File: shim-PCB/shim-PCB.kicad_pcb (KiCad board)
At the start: 2 copper layers, 67.5 x 95.4 mm, 22 parts, among them J1 ROMI-Encoder, J10 LineSensor, J11 LineSensor, J12 SPI, J13 Ultrasonic., J14 THING, J15 THING, J2 ROMI-Encoder, J3 Conn_01x19_Female, J4 ServoAnalog, J5 Conn_01x19_Female, J6 Conn_01x19_Female, J7 ROMI, J8 ROMI, J9 Conn_01x19_Female

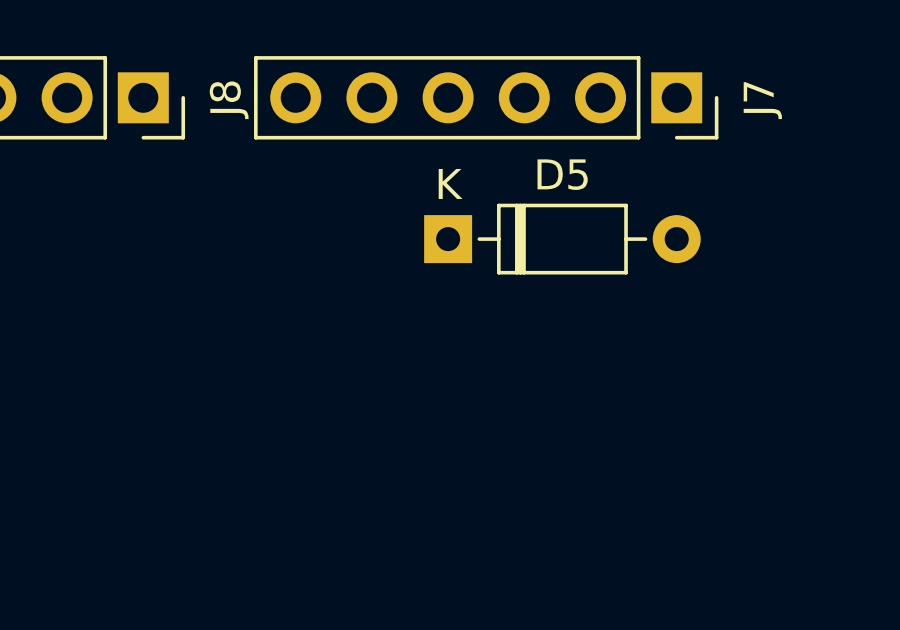
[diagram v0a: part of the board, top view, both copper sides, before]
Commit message: Clamped ~SLP pin and added 02x01 header.
Issue #13
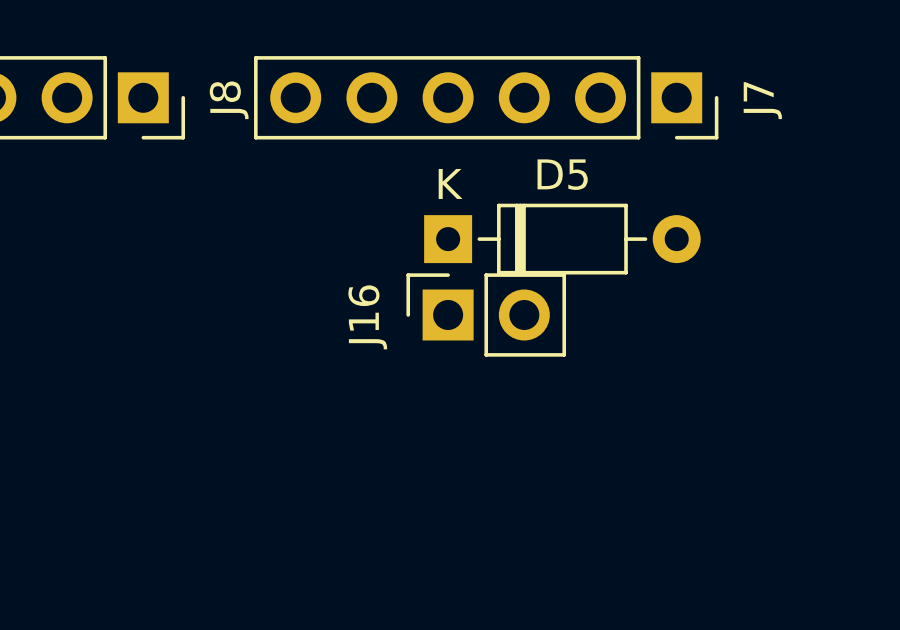
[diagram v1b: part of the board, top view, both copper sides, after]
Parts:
- added J16: Conn_01x02_Female, Connector_PinSocket_2.54mm:PinSocket_1x02_P2.54mm_Vertical, F.Cu at (142.7, 65.2)
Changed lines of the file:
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@@
     (tracks 0)
     (zones 0)
-    (modules 22)
+    (modules 23)
     (nets 48)
   )
@@
       (at (xyz 0 0 0))
       (scale (xyz 1 1 1))
+      (rotate (xyz 0 0 0))
+    )
+  )
+  (module Connector_PinSocket_2.54mm:PinSocket_1x02_P2.54mm_Vertical (layer F.Cu)
+    (at 142.685 65.1844 90)
+    (descr "Through hole straight socket strip, 1x02, 2.54mm pitch, single row (from Kicad 4.0.7), script generated")
+    (tags "Through hole socket strip THT 1x02 2.54mm single row")
+    (fp_text reference J16 (at 0 -2.77 90) (layer F.SilkS)
+      (effects (font (size 1 1) (thickness 0.15)))
+    )
+    (fp_text value Conn_01x02_Female (at 0 5.31 90) (layer F.Fab)
+      (effects (font (size 1 1) (thickness 0.15)))
+    )
+    (fp_line (start -1.27 -1.27) (end 0.635 -1.27) (layer F.Fab) (width 0.1))
+    (fp_line (start 0.635 -1.27) (end 1.27 -0.635) (layer F.Fab) (width 0.1))
+    (fp_line (start 1.27 -0.635) (end 1.27 3.81) (layer F.Fab) (width 0.1))
+    (fp_line (start 1.27 3.81) (end -1.27 3.81) (layer F.Fab) (width 0.1))
+    (fp_line (start -1.27 3.81) (end -1.27 -1.27) (layer F.Fab) (width 0.1))
+    (fp_line (start -1.33 1.27) (end 1.33 1.27) (layer F.SilkS) (width 0.12))
+    (fp_line (start -1.33 1.27) (end -1.33 3.87) (layer F.SilkS) (width 0.12))
+    (fp_line (start -1.33 3.87) (end 1.33 3.87) (layer F.SilkS) (width 0.12))
+    (fp_line (start 1.33 1.27) (end 1.33 3.87) (layer F.SilkS) (width 0.12))
+    (fp_line (start 1.33 -1.33) (end 1.33 0) (layer F.SilkS) (width 0.12))
+    (fp_line (start 0 -1.33) (end 1.33 -1.33) (layer F.SilkS) (width 0.12))
+    (fp_line (start -1.8 -1.8) (end 1.75 -1.8) (layer F.CrtYd) (width 0.05))
+    (fp_line (start 1.75 -1.8) (end 1.75 4.3) (layer F.CrtYd) (width 0.05))
+    (fp_line (start 1.75 4.3) (end -1.8 4.3) (layer F.CrtYd) (width 0.05))
+    (fp_line (start -1.8 4.3) (end -1.8 -1.8) (layer F.CrtYd) (width 0.05))
+    (fp_text user %R (at 0 1.27) (layer F.Fab)
+      (effects (font (size 1 1) (thickness 0.15)))
+    )
+    (pad 1 thru_hole rect (at 0 0 90) (size 1.7 1.7) (drill 1) (layers *.Cu *.Mask)
+      (net 33 GPIO15))
+    (pad 2 thru_hole oval (at 0 2.54 90) (size 1.7 1.7) (drill 1) (layers *.Cu *.Mask)
+      (net 1 GND))
+    (model ${KISYS3DMOD}/Connector_PinSocket_2.54mm.3dshapes/PinSocket_1x02_P2.54mm_Vertical.wrl
+      (at (xyz 0 0 0))
+      (scale (xyz 1 1 1))

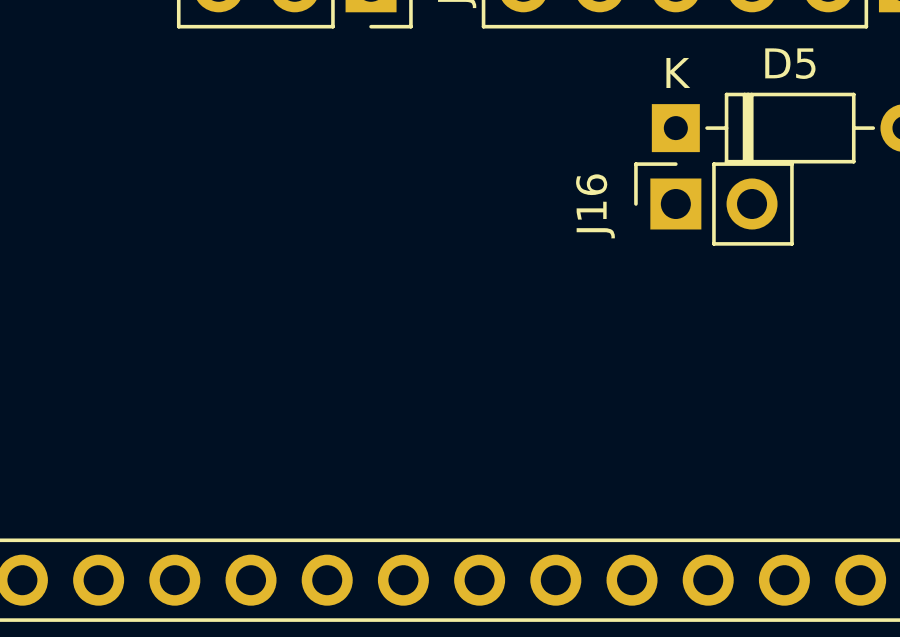
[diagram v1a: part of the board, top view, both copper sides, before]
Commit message: Clamped analog input signal.
Fixed issue #11
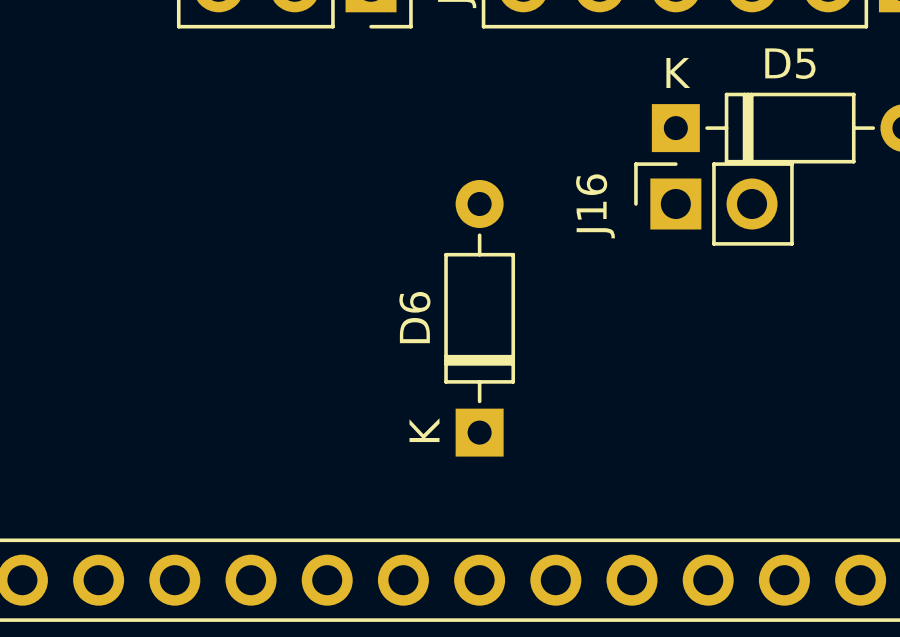
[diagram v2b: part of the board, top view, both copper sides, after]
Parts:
- added D6: D_Zener, Diode_THT:D_DO-35_SOD27_P7.62mm_Horizontal, F.Cu at (136.1, 72.8)
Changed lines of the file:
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@@
     (tracks 0)
     (zones 0)
-    (modules 23)
+    (modules 24)
     (nets 48)
   )
@@
       (at (xyz 0 0 0))
       (scale (xyz 1 1 1))
+      (rotate (xyz 0 0 0))
+    )
+  )
+  (module Diode_THT:D_DO-35_SOD27_P7.62mm_Horizontal (layer F.Cu)
+    (at 136.144 72.8044 90)
+    (descr "Diode, DO-35_SOD27 series, Axial, Horizontal, pin pitch=7.62mm, , length*diameter=4*2mm^2, , http://www.diodes.com/_files/packages/DO-35.pdf")
+    (tags "Diode DO-35_SOD27 series Axial Horizontal pin pitch 7.62mm  length 4mm diameter 2mm")
+    (fp_text reference D6 (at 3.81 -2.12 90) (layer F.SilkS)
+      (effects (font (size 1 1) (thickness 0.15)))
+    )
+    (fp_text value D_Zener (at 3.81 2.12 90) (layer F.Fab)
+      (effects (font (size 1 1) (thickness 0.15)))
+    )
+    (fp_line (start 1.81 -1) (end 1.81 1) (layer F.Fab) (width 0.1))
+    (fp_line (start 1.81 1) (end 5.81 1) (layer F.Fab) (width 0.1))
+    (fp_line (start 5.81 1) (end 5.81 -1) (layer F.Fab) (width 0.1))
+    (fp_line (start 5.81 -1) (end 1.81 -1) (layer F.Fab) (width 0.1))
+    (fp_line (start 0 0) (end 1.81 0) (layer F.Fab) (width 0.1))
+    (fp_line (start 7.62 0) (end 5.81 0) (layer F.Fab) (width 0.1))
+    (fp_line (start 2.41 -1) (end 2.41 1) (layer F.Fab) (width 0.1))
+    (fp_line (start 2.51 -1) (end 2.51 1) (layer F.Fab) (width 0.1))
+    (fp_line (start 2.31 -1) (end 2.31 1) (layer F.Fab) (width 0.1))
+    (fp_line (start 1.69 -1.12) (end 1.69 1.12) (layer F.SilkS) (width 0.12))
+    (fp_line (start 1.69 1.12) (end 5.93 1.12) (layer F.SilkS) (width 0.12))
+    (fp_line (start 5.93 1.12) (end 5.93 -1.12) (layer F.SilkS) (width 0.12))
+    (fp_line (start 5.93 -1.12) (end 1.69 -1.12) (layer F.SilkS) (width 0.12))
+    (fp_line (start 1.04 0) (end 1.69 0) (layer F.SilkS) (width 0.12))
+    (fp_line (start 6.58 0) (end 5.93 0) (layer F.SilkS) (width 0.12))
+    (fp_line (start 2.41 -1.12) (end 2.41 1.12) (layer F.SilkS) (width 0.12))
+    (fp_line (start 2.53 -1.12) (end 2.53 1.12) (layer F.SilkS) (width 0.12))
+    (fp_line (start 2.29 -1.12) (end 2.29 1.12) (layer F.SilkS) (width 0.12))
+    (fp_line (start -1.05 -1.25) (end -1.05 1.25) (layer F.CrtYd) (width 0.05))
+    (fp_line (start -1.05 1.25) (end 8.67 1.25) (layer F.CrtYd) (width 0.05))
+    (fp_line (start 8.67 1.25) (end 8.67 -1.25) (layer F.CrtYd) (width 0.05))
+    (fp_line (start 8.67 -1.25) (end -1.05 -1.25) (layer F.CrtYd) (width 0.05))
+    (fp_text user %R (at 4.11 0 90) (layer F.Fab)
+      (effects (font (size 0.8 0.8) (thickness 0.12)))
+    )
+    (fp_text user K (at 0 -1.8 90) (layer F.Fab)
+      (effects (font (size 1 1) (thickness 0.15)))
+    )
+    (fp_text user K (at 0 -1.8 90) (layer F.SilkS)
+      (effects (font (size 1 1) (thickness 0.15)))
+    )
+    (pad 1 thru_hole rect (at 0 0 90) (size 1.6 1.6) (drill 0.8) (layers *.Cu *.Mask)
+      (net 14 GPIO34))
+    (pad 2 thru_hole oval (at 7.62 0 90) (size 1.6 1.6) (drill 0.8) (layers *.Cu *.Mask)
+      (net 1 GND))
+    (model ${KISYS3DMOD}/Diode_THT.3dshapes/D_DO-35_SOD27_P7.62mm_Horizontal.wrl
+      (at (xyz 0 0 0))
+      (scale (xyz 1 1 1))

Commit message: labeled left-rghtin schematic for motor signals
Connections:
- J7 pad 2: GPIO25 -> GPIO4
- J7 pad 3: GPIO12 -> GPIO13
- J7 pad 5: GPIO4 -> GPIO25
- J7 pad 6: GPIO13 -> GPIO12
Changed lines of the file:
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@@
       (net 33 GPIO15))
     (pad 2 thru_hole oval (at 0 2.54 270) (size 1.7 1.7) (drill 1) (layers *.Cu *.Mask)
-      (net 18 GPIO25))
+      (net 31 GPIO4))
     (pad 3 thru_hole oval (at 0 5.08 270) (size 1.7 1.7) (drill 1) (layers *.Cu *.Mask)
-      (net 22 GPIO12))
+      (net 23 GPIO13))
     (pad 4 thru_hole oval (at 0 7.62 270) (size 1.7 1.7) (drill 1) (layers *.Cu *.Mask)
       (net 33 GPIO15))
     (pad 5 thru_hole oval (at 0 10.16 270) (size 1.7 1.7) (drill 1) (layers *.Cu *.Mask)
-      (net 31 GPIO4))
+      (net 18 GPIO25))
     (pad 6 thru_hole oval (at 0 12.7 270) (size 1.7 1.7) (drill 1) (layers *.Cu *.Mask)
-      (net 23 GPIO13))
+      (net 22 GPIO12))
     (model ${KISYS3DMOD}/Connector_PinSocket_2.54mm.3dshapes/PinSocket_1x06_P2.54mm_Vertical.wrl
       (at (xyz 0 0 0))

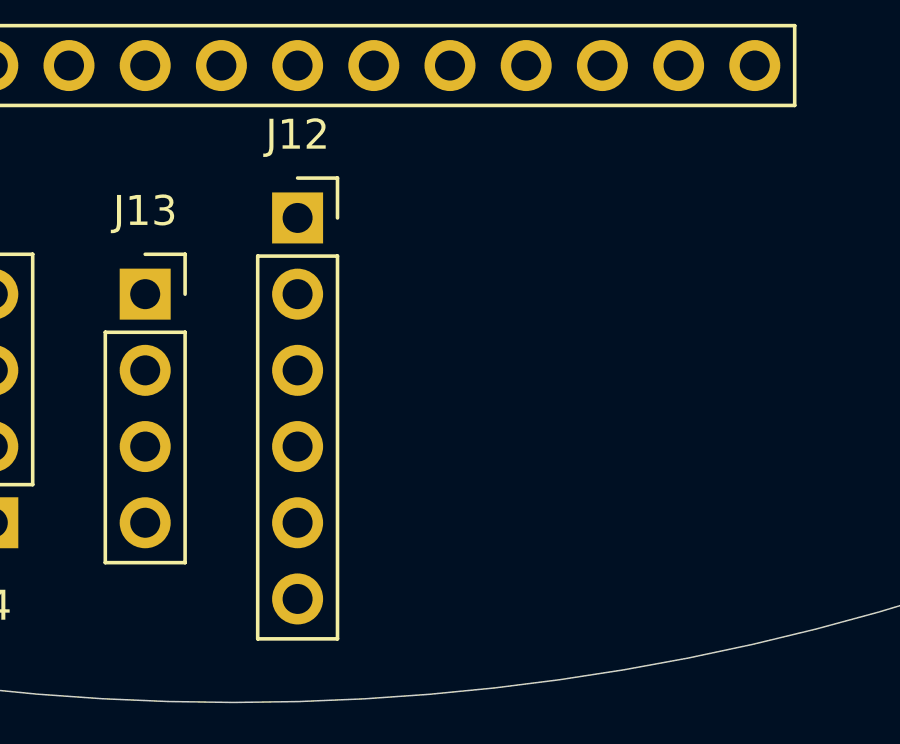
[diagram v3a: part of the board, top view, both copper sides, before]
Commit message: Broke out i2c
ISsue #7
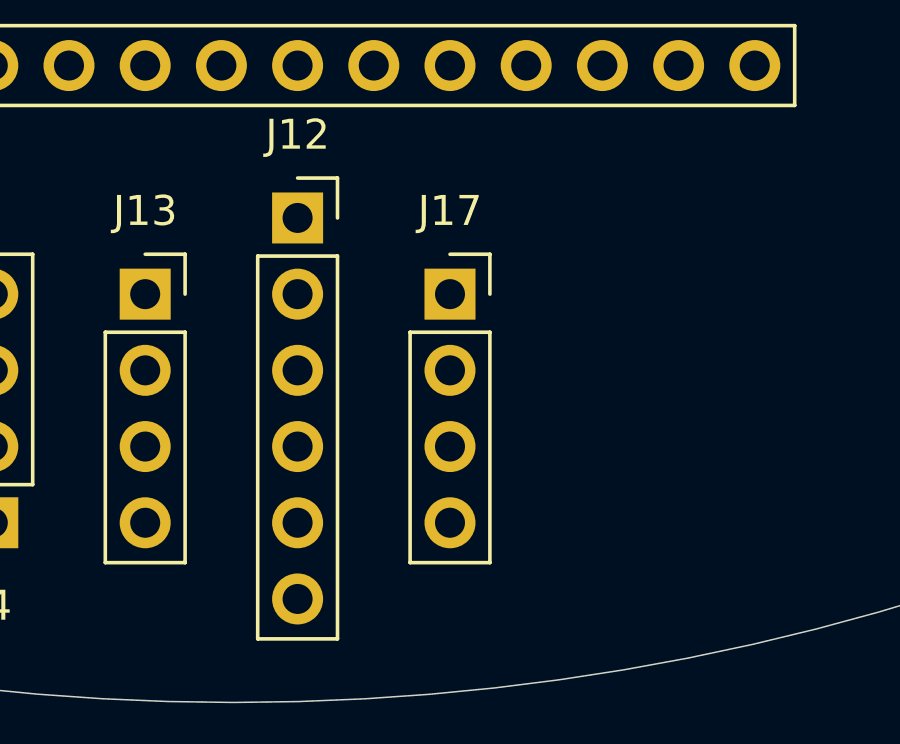
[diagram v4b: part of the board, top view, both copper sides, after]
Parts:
- added J17: i2c, Connector_PinSocket_2.54mm:PinSocket_1x04_P2.54mm_Vertical, F.Cu at (148.8, 129.8)
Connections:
- J12 pad 5: GPIO15 -> GPIO5
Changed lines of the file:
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@@
     (tracks 0)
     (zones 0)
-    (modules 24)
+    (modules 25)
     (nets 48)
   )
@@
       (net 5 GPIO18))
     (pad 5 thru_hole oval (at 0 10.16) (size 1.7 1.7) (drill 1) (layers *.Cu *.Mask)
-      (net 33 GPIO15))
+      (net 30 GPIO5))
     (pad 6 thru_hole oval (at 0 12.7) (size 1.7 1.7) (drill 1) (layers *.Cu *.Mask)
       (net 1 GND))
@@
       (at (xyz 0 0 0))
       (scale (xyz 1 1 1))
+      (rotate (xyz 0 0 0))
+    )
+  )
+  (module Connector_PinSocket_2.54mm:PinSocket_1x04_P2.54mm_Vertical (layer F.Cu)
+    (at 148.844 129.794)
+    (descr "Through hole straight socket strip, 1x04, 2.54mm pitch, single row (from Kicad 4.0.7), script generated")
+    (tags "Through hole socket strip THT 1x04 2.54mm single row")
+    (fp_text reference J17 (at 0 -2.77) (layer F.SilkS)
+      (effects (font (size 1 1) (thickness 0.15)))
+    )
+    (fp_text value i2c (at 0 10.39) (layer F.Fab)
+      (effects (font (size 1 1) (thickness 0.15)))
+    )
+    (fp_line (start -1.27 -1.27) (end 0.635 -1.27) (layer F.Fab) (width 0.1))
+    (fp_line (start 0.635 -1.27) (end 1.27 -0.635) (layer F.Fab) (width 0.1))
+    (fp_line (start 1.27 -0.635) (end 1.27 8.89) (layer F.Fab) (width 0.1))
+    (fp_line (start 1.27 8.89) (end -1.27 8.89) (layer F.Fab) (width 0.1))
+    (fp_line (start -1.27 8.89) (end -1.27 -1.27) (layer F.Fab) (width 0.1))
+    (fp_line (start -1.33 1.27) (end 1.33 1.27) (layer F.SilkS) (width 0.12))
+    (fp_line (start -1.33 1.27) (end -1.33 8.95) (layer F.SilkS) (width 0.12))
+    (fp_line (start -1.33 8.95) (end 1.33 8.95) (layer F.SilkS) (width 0.12))
+    (fp_line (start 1.33 1.27) (end 1.33 8.95) (layer F.SilkS) (width 0.12))
+    (fp_line (start 1.33 -1.33) (end 1.33 0) (layer F.SilkS) (width 0.12))
+    (fp_line (start 0 -1.33) (end 1.33 -1.33) (layer F.SilkS) (width 0.12))
+    (fp_line (start -1.8 -1.8) (end 1.75 -1.8) (layer F.CrtYd) (width 0.05))
+    (fp_line (start 1.75 -1.8) (end 1.75 9.4) (layer F.CrtYd) (width 0.05))
+    (fp_line (start 1.75 9.4) (end -1.8 9.4) (layer F.CrtYd) (width 0.05))
+    (fp_line (start -1.8 9.4) (end -1.8 -1.8) (layer F.CrtYd) (width 0.05))
+    (fp_text user %R (at 0 3.81 90) (layer F.Fab)
+      (effects (font (size 1 1) (thickness 0.15)))
+    )
+    (pad 1 thru_hole rect (at 0 0) (size 1.7 1.7) (drill 1) (layers *.Cu *.Mask)
+      (net 34 +3V3))
+    (pad 2 thru_hole oval (at 0 2.54) (size 1.7 1.7) (drill 1) (layers *.Cu *.Mask)
+      (net 29 GPIO21))
+    (pad 3 thru_hole oval (at 0 5.08) (size 1.7 1.7) (drill 1) (layers *.Cu *.Mask)
+      (net 26 GPIO22))
+    (pad 4 thru_hole oval (at 0 7.62) (size 1.7 1.7) (drill 1) (layers *.Cu *.Mask)
+      (net 1 GND))
+    (model ${KISYS3DMOD}/Connector_PinSocket_2.54mm.3dshapes/PinSocket_1x04_P2.54mm_Vertical.wrl
+      (at (xyz 0 0 0))
+      (scale (xyz 1 1 1))

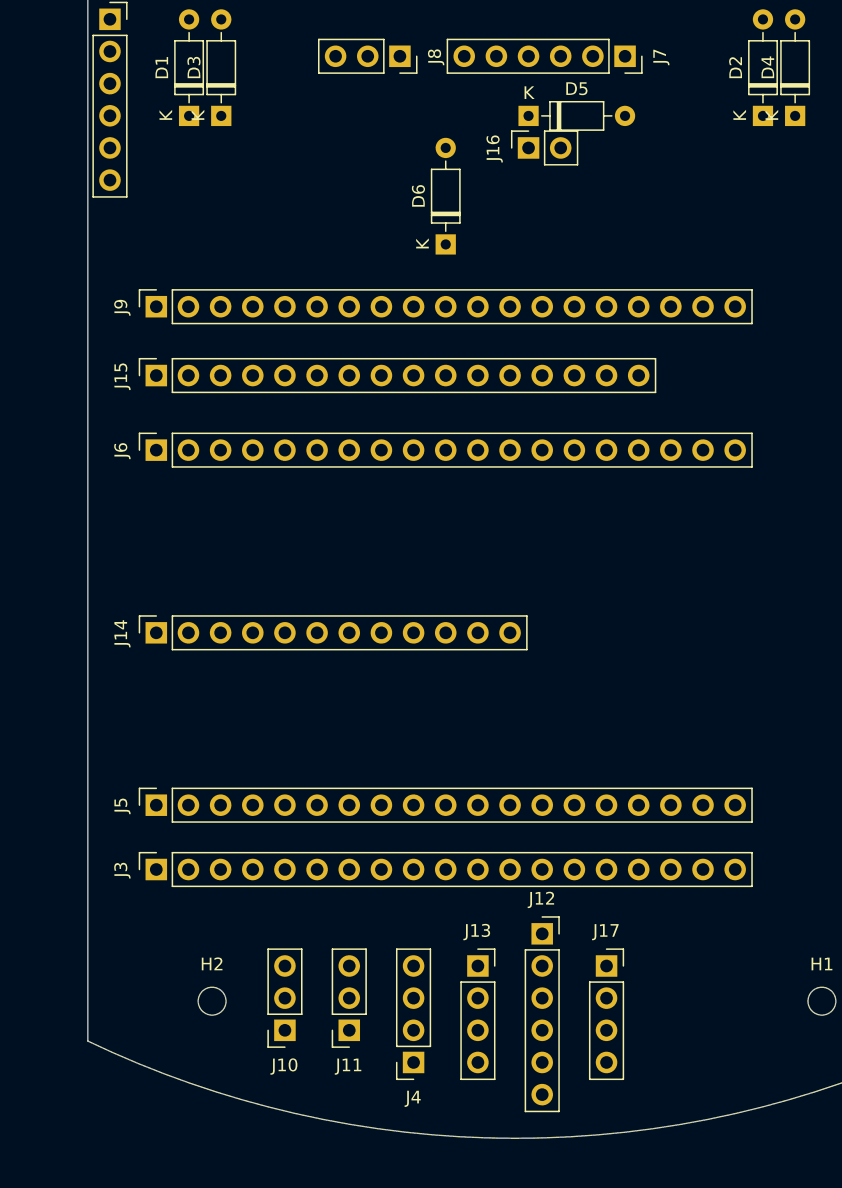
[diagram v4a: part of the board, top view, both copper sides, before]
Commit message: Made more room for labels
Issue #14
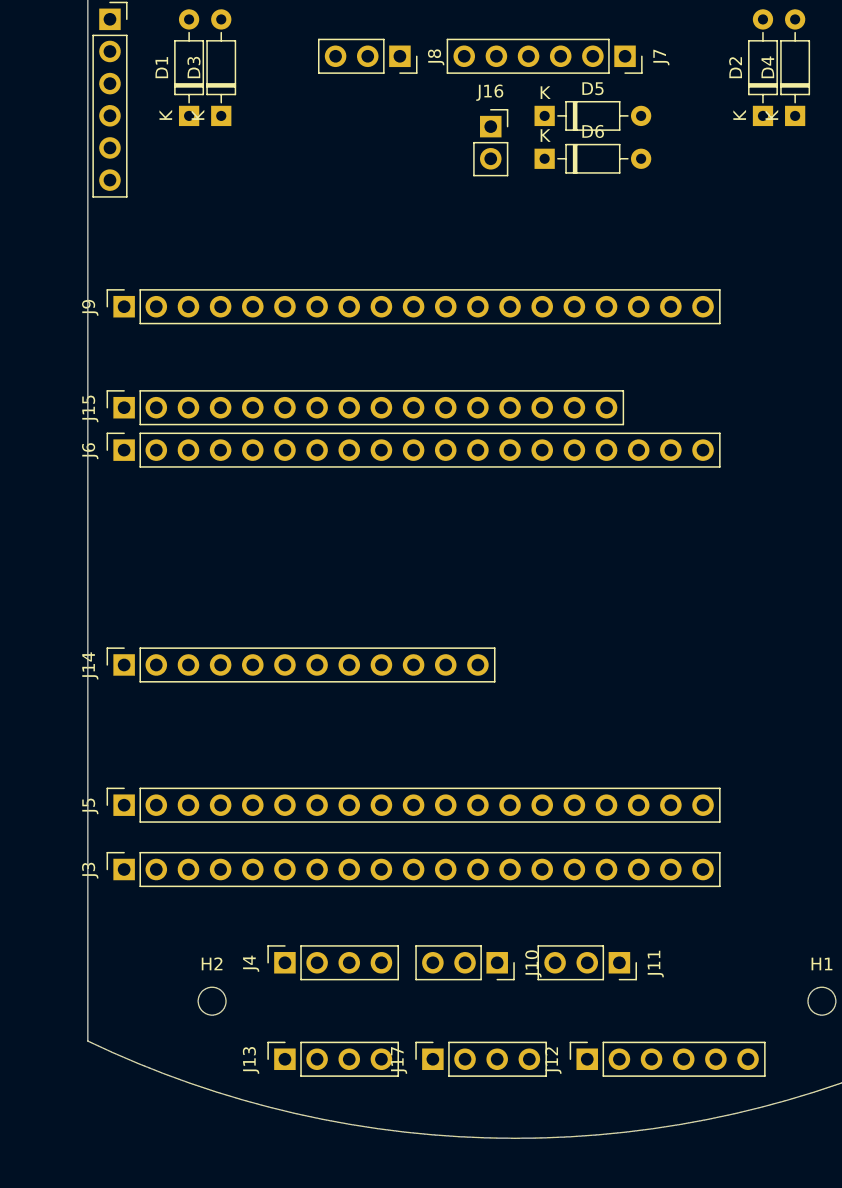
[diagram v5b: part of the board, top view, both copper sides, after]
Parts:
- moved J11 22.0 mm to (149.9, 129.5), turned to 270 degrees
- moved J10 17.6 mm to (140.2, 129.5), turned to 270 degrees
- moved J13 16.9 mm to (123.4, 137.2), turned to 90 degrees
- moved J17 15.6 mm to (135.1, 137.2), turned to 90 degrees
- moved J4 12.9 mm to (123.4, 129.5), turned to 90 degrees
- moved J12 10.5 mm to (147.3, 137.2), turned to 90 degrees
- moved D6 10.3 mm to (144.0, 66.0), turned to 0 degrees
- moved J15 3.59 mm to (110.7, 85.7)
- moved J14 3.59 mm to (110.7, 106.0)
- moved J16 3.43 mm to (139.7, 63.5), turned to 0 degrees
- moved J3 2.54 mm to (110.7, 122.2)
- moved J5 2.54 mm to (110.7, 117.1)
- moved J6 2.54 mm to (110.7, 89.1)
- moved J9 2.54 mm to (110.7, 77.7)
- moved D5 1.27 mm to (144.0, 62.7)
